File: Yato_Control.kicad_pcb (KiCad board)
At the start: 2 copper layers, 12 parts, among them J1 Conn_01x04, J2 Conn_01x04, J3 Conn_01x04, U1 LTV-827, U3 4053

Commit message: initial layout done Signed-off-by: Sir Quickly <sir.quickly0@googlemail.com>
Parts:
- added C3: 100n, Capacitor_THT:C_Disc_D3.0mm_W1.6mm_P2.50mm, F.Cu at (128.6, 55.2)
- added C4: 4u7, Capacitor_THT:CP_Radial_D5.0mm_P2.50mm, F.Cu at (144.9, 50.5)
- added H1: MountingHole, MountingHole:MountingHole_4mm, F.Cu at (99.7, 23.4)
- added H2: MountingHole, MountingHole:MountingHole_4mm, F.Cu at (99.7, 69.4)
- added H3: MountingHole, MountingHole:MountingHole_4mm, F.Cu at (154.7, 69.4)
- added H4: MountingHole, MountingHole:MountingHole_4mm, F.Cu at (154.7, 23.4)
- C1: value CP -> 100uF; footprint Capacitor_THT:CP_Radial_D10.0mm_P5.00mm -> Capacitor_THT:CP_Radial_D10.0mm_P2.50mm_P5.00mm
- C2: value C -> 100n
- R3: value 100R -> 4k7
- R4: value 10k -> 1k0
- moved R5 113.2 mm to (131.3, 43.3)
- moved J2 90.7 mm to (153.2, 39.5), turned to 90 degrees
- moved R3 79.8 mm to (124.7, 42.9), turned to 270 degrees
- moved R4 79.3 mm to (131.2, 47.7)
- moved J3 77.3 mm to (153.1, 61.3)
- moved C2 64.2 mm to (144.8, 45.1), turned to 0 degrees
- moved U3 56.6 mm to (128.2, 20.9)
- moved C1 53.1 mm to (136.9, 57.3), turned to 90 degrees
- moved R1 48.9 mm to (105.5, 32.1), turned to 0 degrees
- moved R2 43.9 mm to (105.3, 38.5), turned to 0 degrees
- moved U1 42.1 mm to (116.7, 32.1)
- moved J1 39.0 mm to (101.0, 33.6)
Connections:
- R3 pad 1: +5V -> Net-(R3-Pad1)
- R3 pad 2: Net-(R3-Pad2) -> Net-(C1-Pad1)
- U1 pad 5: Net-(C1-Pad1) -> Net-(R3-Pad1)
- U1 pad 6: Net-(R3-Pad2) -> +5V
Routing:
- net GND: track 0.00 -> 87.4 mm
- net +5V: track 0.00 -> 78.0 mm
- net Net-(C1-Pad1): track 0.00 -> 52.9 mm, vias 0 -> 1
- net /Pwr_Ctrl_Chassis: track 0.00 -> 44.0 mm, vias 0 -> 1
- net /On_Chassis: track 0.00 -> 43.1 mm, vias 0 -> 1
- net /Power_Ctrl_Int: track 0.00 -> 31.7 mm, vias 0 -> 1
- net Net-(R5-Pad2): track 0.00 -> 29.2 mm, vias 0 -> 2
- net /On_Int: track 0.00 -> 25.0 mm, vias 0 -> 1
- net /Pwr_Ctrl_Ext: track 0.00 -> 18.6 mm
- net /On_Ext: track 0.00 -> 16.1 mm
- net +5VD: track 0.00 -> 10.8 mm
- net Net-(R2-Pad2): track 0.00 -> 4.33 mm
- net Net-(R1-Pad2): track 0.00 -> 3.58 mm
- net Net-(R3-Pad1): track 0.00 -> 3.37 mm
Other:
- board outline added: 65 x 56 mm
- net class Default: trace_width 0.25 -> 0.5
- board text added: "Control Knob"
- board text added: "Display PCB"
- board text added: "YATO Control V1.0"
- board text added: "ext. control"

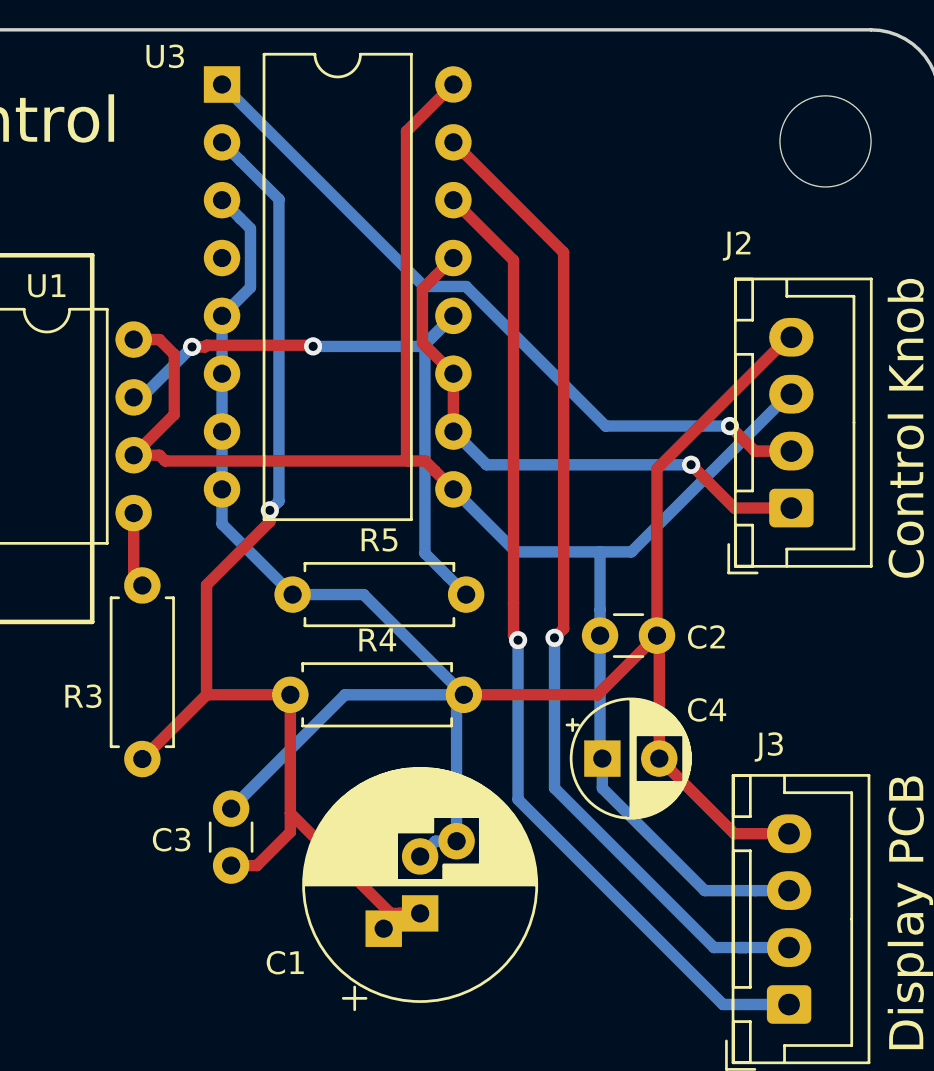
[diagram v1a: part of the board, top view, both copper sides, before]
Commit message: - Pulldown Widerstand für das On-Signal von der YATO Poti-Platine - Pos. R4 korrigiert
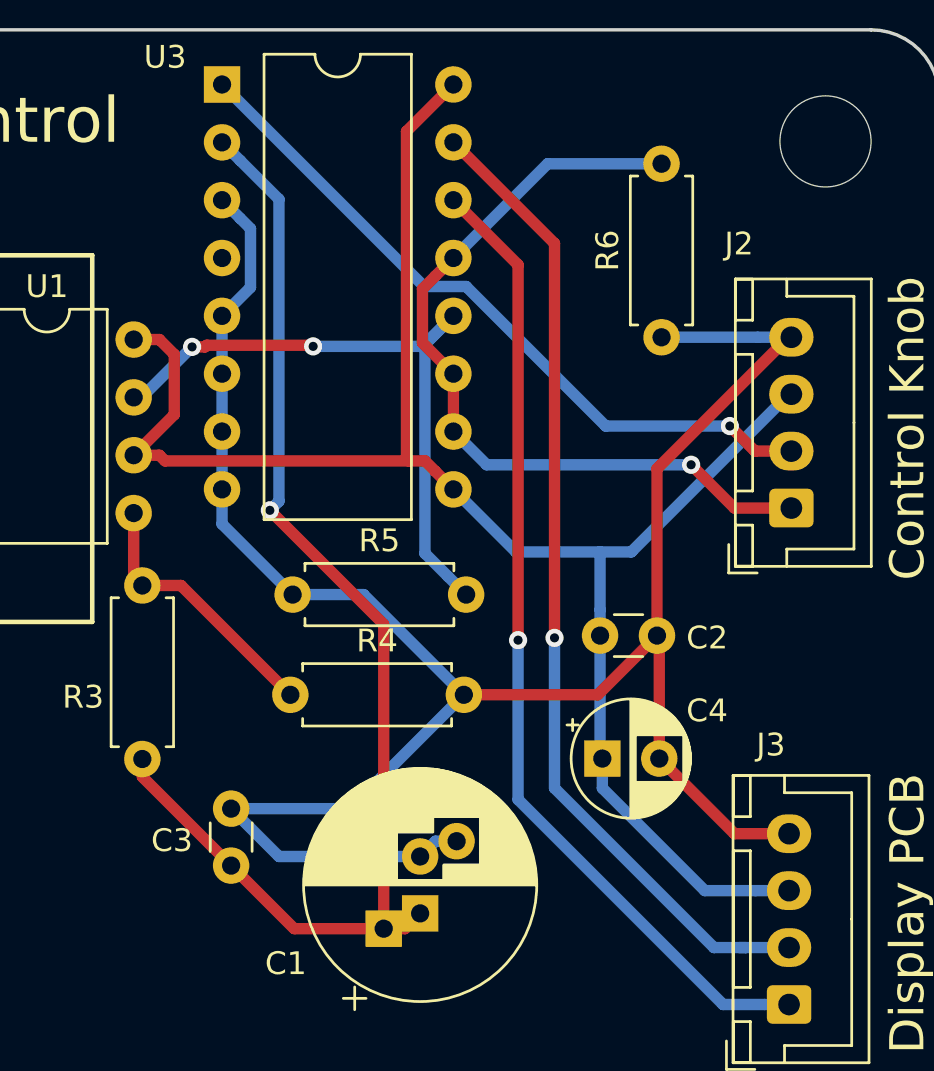
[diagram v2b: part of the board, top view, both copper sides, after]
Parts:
- added R6: 4k7, Resistor_THT:R_Axial_DIN0207_L6.3mm_D2.5mm_P7.62mm_Horizontal, F.Cu at (147.5, 32.0)
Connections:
- R4 pad 1: Net-(C1-Pad1) -> Net-(R3-Pad1)
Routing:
- net /On_Int: track 25.0 -> 35.8 mm
- net GND: track 87.4 -> 96.2 mm
- net Net-(R3-Pad1): track 3.37 -> 11.2 mm
- net Net-(C1-Pad1): track 52.9 -> 53.8 mm
